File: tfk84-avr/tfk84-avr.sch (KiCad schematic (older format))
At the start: 31 parts, among them J1 USB_C_Receptacle_USB2.0, J2 AVR-ISP-6, SW1 Reset, U1 ATmega32U4-AU, Y1 16MHz

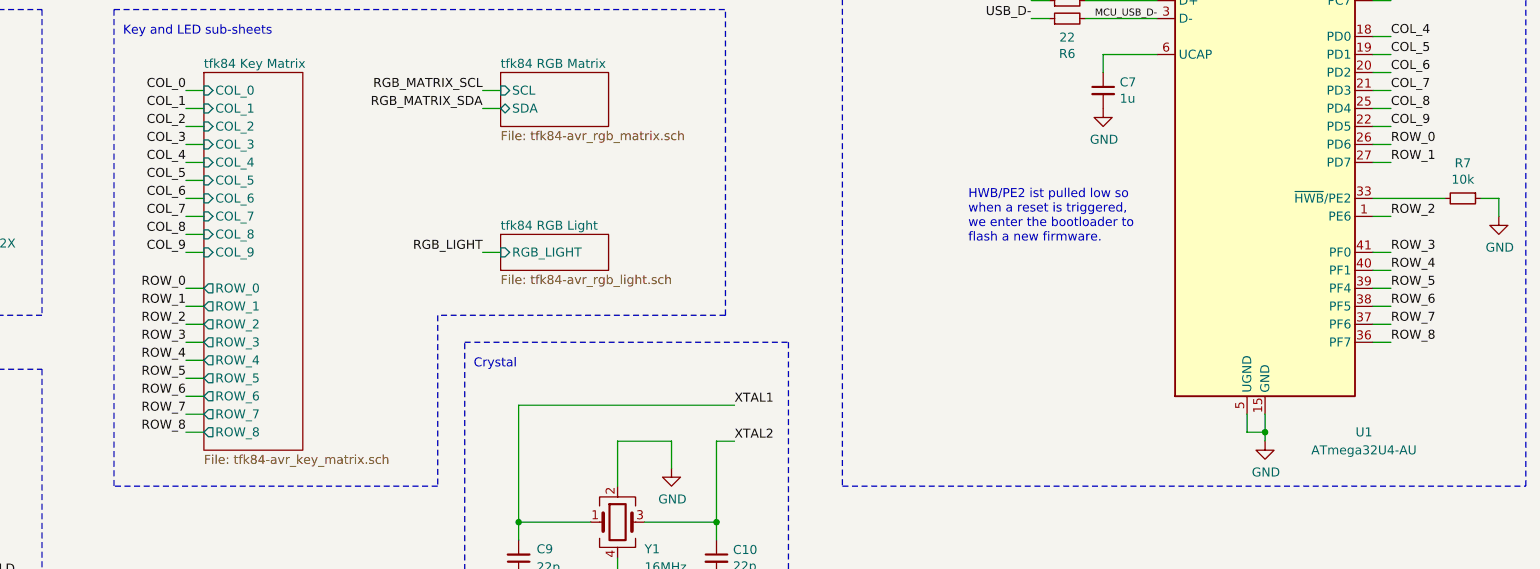
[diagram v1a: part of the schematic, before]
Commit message: Change key matrix to 12x7
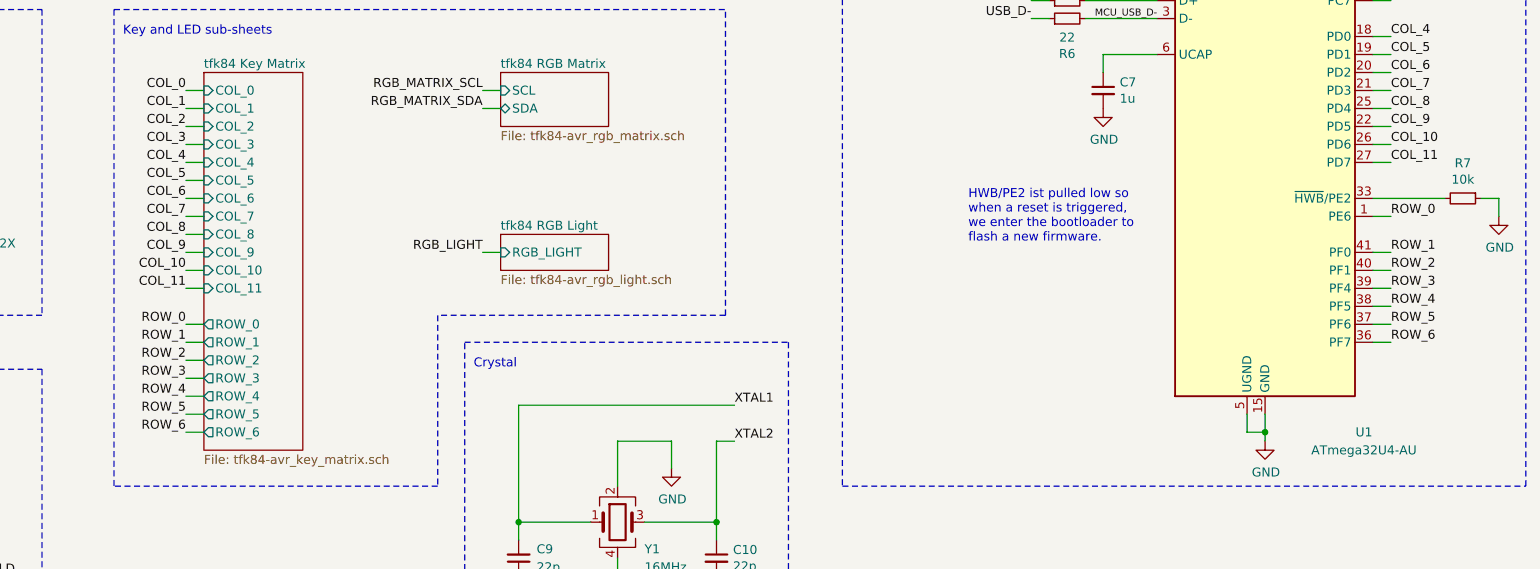
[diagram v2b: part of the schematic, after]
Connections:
- net ROW_7 is gone; now on net ROW_5: U1.37 (PF6)
- net ROW_8 is gone; now on net ROW_6: U1.36 (PF7)
- net ROW_0: now also U1.1 (PE6); no longer U1.26 (PD6)
- net ROW_1: now also U1.41 (PF0); no longer U1.27 (PD7)
- net ROW_2: now also U1.40 (PF1); no longer U1.1 (PE6)
- net ROW_3: now also U1.39 (PF4); no longer U1.41 (PF0)
- net ROW_4: now also U1.38 (PF5); no longer U1.40 (PF1)
- net ROW_5: no longer U1.39 (PF4)
- net ROW_6: no longer U1.38 (PF5)
- new net COL_10: U1.26 (PD6)
- new net COL_11: U1.27 (PD7)
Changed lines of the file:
@@
 	3550 4550 3450 4550
 Wire Wire Line
-	3550 5350 3450 5350
-Wire Wire Line
-	3550 5450 3450 5450
-Wire Wire Line
-	3450 5550 3550 5550
-Wire Wire Line
-	3550 5650 3450 5650
+	3550 5550 3450 5550
 Wire Wire Line
 	3450 5750 3550 5750
-Text Label 3450 5350 2    50   ~ 0
+Wire Wire Line
+	3550 5850 3450 5850
+Wire Wire Line
+	3450 5950 3550 5950
+Text Label 3450 5550 2    50   ~ 0
 ROW_0
-Text Label 3450 5450 2    50   ~ 0
+Text Label 3450 5650 2    50   ~ 0
 ROW_1
-Text Label 3450 5550 2    50   ~ 0
+Text Label 3450 5750 2    50   ~ 0
 ROW_2
-Text Label 3450 5650 2    50   ~ 0
+Text Label 3450 5850 2    50   ~ 0
 ROW_3
-Text Label 3450 5750 2    50   ~ 0
+Text Label 3450 5950 2    50   ~ 0
 ROW_4
 Text Label 3450 4250 2    50   ~ 0
@@
 	700  -250 700  -1250
 Wire Wire Line
-	3550 5850 3450 5850
-Text Label 3450 5850 2    50   ~ 0
+	3550 6050 3450 6050
+Text Label 3450 6050 2    50   ~ 0
 ROW_5
 Connection ~ 1150 2800
@@
 	10050 4150 10150 4150
 Text Label 10150 5650 0    50   ~ 0
-ROW_8
+ROW_6
+Text Label 10150 5350 0    50   ~ 0
+ROW_3
 Text Label 10150 5550 0    50   ~ 0
-ROW_7
+ROW_5
 Text Label 10150 5450 0    50   ~ 0
-ROW_6
+ROW_4
+Text Label 10150 5250 0    50   ~ 0
+ROW_2
 Text Label 10150 5150 0    50   ~ 0
-ROW_3
-Text Label 10150 5350 0    50   ~ 0
-ROW_5
-Text Label 10150 5250 0    50   ~ 0
-ROW_4
+ROW_1
 Text Label 10150 4950 0    50   ~ 0
-ROW_2
-Text Label 10150 4650 0    50   ~ 0
-ROW_1
-Text Label 10150 4550 0    50   ~ 0
 ROW_0
 $Sheet
@@
 F4 "COL_2" I L 3550 4450 50
 F5 "COL_3" I L 3550 4550 50
-F6 "ROW_0" O L 3550 5350 50
-F7 "ROW_1" O L 3550 5450 50
-F8 "ROW_2" O L 3550 5550 50
-F9 "ROW_3" O L 3550 5650 50
-F10 "ROW_4" O L 3550 5750 50
-F11 "ROW_5" O L 3550 5850 50
+F6 "ROW_0" O L 3550 5550 50
+F7 "ROW_1" O L 3550 5650 50
+F8 "ROW_2" O L 3550 5750 50
+F9 "ROW_3" O L 3550 5850 50
+F10 "ROW_4" O L 3550 5950 50
+F11 "ROW_5" O L 3550 6050 50
 F12 "COL_4" I L 3550 4650 50
 F13 "COL_5" I L 3550 4750 50
@@
 F16 "COL_8" I L 3550 5050 50
 F17 "COL_9" I L 3550 5150 50
-F18 "ROW_6" O L 3550 5950 50
-F19 "ROW_7" O L 3550 6050 50
-F20 "ROW_8" O L 3550 6150 50
+F18 "ROW_6" O L 3550 6150 50
+F19 "COL_10" I L 3550 5250 50
+F20 "COL_11" I L 3550 5350 50
 $EndSheet
-Wire Wire Line
-	3550 5950 3450 5950
-Wire Wire Line
-	3450 6050 3550 6050
-Wire Wire Line
-	3550 6150 3450 6150
-Text Label 3450 5950 2    50   ~ 0
-ROW_6
-Text Label 3450 6050 2    50   ~ 0
-ROW_7
-Text Label 3450 6150 2    50   ~ 0
-ROW_8
 Text Label 3450 4650 2    50   ~ 0
 COL_4
@@
 Wire Notes Line
 	3050 3800 3050 6450
+Text Label 3450 6150 2    50   ~ 0
+ROW_6
+Wire Wire Line
+	3450 6150 3550 6150
+Wire Wire Line
+	3450 5650 3550 5650
+Wire Wire Line
+	3450 5250 3550 5250
+Wire Wire Line
+	3450 5350 3550 5350
+Text Label 3450 5250 2    50   ~ 0
+COL_10
+Text Label 3450 5350 2    50   ~ 0
+COL_11
+Text Label 10150 4550 0    50   ~ 0
+COL_10
+Text Label 10150 4650 0    50   ~ 0
+COL_11
 $EndSCHEMATC

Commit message: Continue layout
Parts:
- added H10, H11, H9: MountingHole, MountingHole:MountingHole_2.5mm_Pad, symbol Mechanical:MountingHole
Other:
- moved on the sheet: C8, D3, H1, H2, H3, H4, R8
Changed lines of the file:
@@
 L Device:D_Small D3
 U 1 1 60989164
-P 1350 6550
+P 1500 6300
 AR Path="/60989164" Ref="D3"  Part="1"
 AR Path="/60815FFC/60989164" Ref="D?"  Part="1"
-F 0 "D3" H 1350 6450 50  0000 C CNN
-F 1 "Case ESD" H 1350 6434 50  0001 C CNN
-F 2 "Diode_SMD:D_SOD-123" V 1350 6550 50  0001 C CNN
-F 3 "~" V 1350 6550 50  0001 C CNN
-	1    1350 6550
+F 0 "D3" H 1500 6200 50  0000 C CNN
+F 1 "Case ESD" H 1500 6184 50  0001 C CNN
+F 2 "Diode_SMD:D_SOD-123" V 1500 6300 50  0001 C CNN
+F 3 "~" V 1500 6300 50  0001 C CNN
+	1    1500 6300
 	-1   0    0    1
 $EndComp
 Wire Wire Line
-	1450 6550 1550 6550
-Wire Wire Line
-	1550 6550 1550 6650
-Wire Wire Line
-	1550 6550 1900 6550
-Wire Wire Line
-	1900 6550 1900 6650
-Connection ~ 1550 6550
+	1600 6300 1700 6300
+Wire Wire Line
+	1700 6300 1700 6400
+Wire Wire Line
+	1700 6300 2050 6300
+Wire Wire Line
+	2050 6300 2050 6400
+Connection ~ 1700 6300
 $Comp
 L Device:R_Small R8
 U 1 1 6098916F
-P 1550 6750
+P 1700 6500
 AR Path="/6098916F" Ref="R8"  Part="1"
 AR Path="/60815FFC/6098916F" Ref="R?"  Part="1"
-F 0 "R8" H 1609 6796 50  0000 L CNN
-F 1 "1M" H 1609 6705 50  0000 L CNN
-F 2 "Resistor_SMD:R_0805_2012Metric_Pad1.20x1.40mm_HandSolder" H 1550 6750 50  0001 C CNN
-F 3 "~" H 1550 6750 50  0001 C CNN
-	1    1550 6750
+F 0 "R8" H 1759 6546 50  0000 L CNN
+F 1 "1M" H 1759 6455 50  0000 L CNN
+F 2 "Resistor_SMD:R_0805_2012Metric_Pad1.20x1.40mm_HandSolder" H 1700 6500 50  0001 C CNN
+F 3 "~" H 1700 6500 50  0001 C CNN
+	1    1700 6500
 	1    0    0    -1
 $EndComp
@@
 L Device:C_Small C8
 U 1 1 60989175
-P 1900 6750
+P 2050 6500
 AR Path="/60989175" Ref="C8"  Part="1"
 AR Path="/60815FFC/60989175" Ref="C?"  Part="1"
-F 0 "C8" H 1992 6796 50  0000 L CNN
-F 1 "4.7n" H 1992 6705 50  0000 L CNN
-F 2 "Capacitor_SMD:C_0805_2012Metric_Pad1.18x1.45mm_HandSolder" H 1900 6750 50  0001 C CNN
-F 3 "~" H 1900 6750 50  0001 C CNN
-	1    1900 6750
-	1    0    0    -1
-$EndComp
-Wire Wire Line
-	1900 6850 1900 6950
-Wire Wire Line
-	1900 6950 1550 6950
-Wire Wire Line
-	1550 6950 1550 6850
-Text Notes 750  5950 0    50   ~ 0
+F 0 "C8" H 2142 6546 50  0000 L CNN
+F 1 "4.7n" H 2142 6455 50  0000 L CNN
+F 2 "Capacitor_SMD:C_0805_2012Metric_Pad1.18x1.45mm_HandSolder" H 2050 6500 50  0001 C CNN
+F 3 "~" H 2050 6500 50  0001 C CNN
+	1    2050 6500
+	1    0    0    -1
+$EndComp
+Wire Wire Line
+	2050 6600 2050 6700
+Wire Wire Line
+	2050 6700 1700 6700
+Wire Wire Line
+	1700 6700 1700 6600
+Text Notes 900  5900 0    50   ~ 0
 Mounting holes and ESD inrush protection
 Wire Notes Line
-	700  5800 2650 5800
-Wire Notes Line
-	2650 5800 2650 7600
-Wire Notes Line
-	2650 7600 700  7600
-Wire Notes Line
-	700  7600 700  5800
-Wire Wire Line
-	1250 6550 1050 6550
+	700  5750 2800 5750
+Wire Notes Line
+	2800 5750 2800 7550
+Wire Notes Line
+	2800 7550 700  7550
+Wire Notes Line
+	700  7550 700  5750
+Wire Wire Line
+	1400 6300 1200 6300
 $Comp
 L Mechanical:MountingHole_Pad H2
 U 1 1 60989184
-P 950 6550
+P 1100 6300
 AR Path="/60989184" Ref="H2"  Part="1"
 AR Path="/60815FFC/60989184" Ref="H?"  Part="1"
-F 0 "H2" V 800 6600 50  0000 C CNN
-F 1 "Case" V 700 6600 50  0000 C CNN
-F 2 "MountingHole:MountingHole_2.5mm_Pad" H 950 6550 50  0001 C CNN
-F 3 "~" H 950 6550 50  0001 C CNN
-	1    950  6550
+F 0 "H2" V 1100 6500 50  0000 C CNN
+F 1 "Case" V 1000 6500 50  0000 C CNN
+F 2 "MountingHole:MountingHole_2.5mm_Pad" H 1100 6300 50  0001 C CNN
+F 3 "~" H 1100 6300 50  0001 C CNN
+	1    1100 6300
 	0    -1   -1   0
 $EndComp
 Wire Wire Line
-	1900 6950 2250 6950
-Connection ~ 1900 6950
-Text Label 2250 6950 0    50   ~ 0
+	2050 6700 2400 6700
+Connection ~ 2050 6700
+Text Label 2400 6700 0    50   ~ 0
 SHIELD
-Text Notes 1600 7300 0    50   ~ 0
+Text Notes 1750 7050 0    50   ~ 0
 Shunt ESD away from \nGND and ICs to USB \nshield.
 Wire Wire Line
@@
 L Mechanical:MountingHole H1
 U 1 1 60BC9C45
-P 900 6150
-F 0 "H1" H 850 6000 50  0000 L CNN
-F 1 "MountingHole" H 800 5900 50  0001 L CNN
-F 2 "MountingHole:MountingHole_2.5mm_Pad" H 900 6150 50  0001 C CNN
-F 3 "~" H 900 6150 50  0001 C CNN
-	1    900  6150
+P 1050 6100
+F 0 "H1" H 850 6100 50  0000 L CNN
+F 1 "MountingHole" H 950 5850 50  0001 L CNN
+F 2 "MountingHole:MountingHole_2.5mm_Pad" H 1050 6100 50  0001 C CNN
+F 3 "~" H 1050 6100 50  0001 C CNN
+	1    1050 6100
 	1    0    0    -1
 $EndComp
@@
 L Mechanical:MountingHole H3
 U 1 1 60BCA1EE
-P 900 6950
-F 0 "H3" H 850 6800 50  0000 L CNN
-F 1 "MountingHole" H 1000 6905 50  0001 L CNN
-F 2 "MountingHole:MountingHole_2.5mm_Pad" H 900 6950 50  0001 C CNN
-F 3 "~" H 900 6950 50  0001 C CNN
-	1    900  6950
+P 1050 6500
+F 0 "H3" H 850 6500 50  0000 L CNN
+F 1 "MountingHole" H 1150 6455 50  0001 L CNN
+F 2 "MountingHole:MountingHole_2.5mm_Pad" H 1050 6500 50  0001 C CNN
+F 3 "~" H 1050 6500 50  0001 C CNN
+	1    1050 6500
 	1    0    0    -1
 $EndComp
@@
 L Mechanical:MountingHole H4
 U 1 1 60BCA526
-P 900 7350
-F 0 "H4" H 850 7200 50  0000 L CNN
-F 1 "MountingHole" H 1000 7305 50  0001 L CNN
-F 2 "MountingHole:MountingHole_2.5mm_Pad" H 900 7350 50  0001 C CNN
-F 3 "~" H 900 7350 50  0001 C CNN
-	1    900  7350
+P 1050 6700
+F 0 "H4" H 850 6700 50  0000 L CNN
+F 1 "MountingHole" H 1150 6655 50  0001 L CNN
+F 2 "MountingHole:MountingHole_2.5mm_Pad" H 1050 6700 50  0001 C CNN
+F 3 "~" H 1050 6700 50  0001 C CNN
+	1    1050 6700
 	1    0    0    -1
 $EndComp
@@
 Text Label 10150 4650 0    50   ~ 0
 COL_11
+$Comp
+L Mechanical:MountingHole H9
+U 1 1 60FF3666
+P 1050 6900
+F 0 "H9" H 850 6900 50  0000 L CNN
+F 1 "MountingHole" H 1150 6855 50  0001 L CNN
+F 2 "MountingHole:MountingHole_2.5mm_Pad" H 1050 6900 50  0001 C CNN
+F 3 "~" H 1050 6900 50  0001 C CNN
+	1    1050 6900
+	1    0    0    -1
+$EndComp
+$Comp
+L Mechanical:MountingHole H10
+U 1 1 60FF38B8
+P 1050 7100
+F 0 "H10" H 800 7100 50  0000 L CNN
+F 1 "MountingHole" H 1150 7055 50  0001 L CNN
+F 2 "MountingHole:MountingHole_2.5mm_Pad" H 1050 7100 50  0001 C CNN
+F 3 "~" H 1050 7100 50  0001 C CNN
+	1    1050 7100
+	1    0    0    -1
+$EndComp
+$Comp
+L Mechanical:MountingHole H11
+U 1 1 60FF3AA3
+P 1050 7300
+F 0 "H11" H 800 7300 50  0000 L CNN
+F 1 "MountingHole" H 1150 7255 50  0001 L CNN
+F 2 "MountingHole:MountingHole_2.5mm_Pad" H 1050 7300 50  0001 C CNN
+F 3 "~" H 1050 7300 50  0001 C CNN
+	1    1050 7300
+	1    0    0    -1
+$EndComp
 $EndSCHEMATC

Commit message: Continue layout
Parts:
- H1: renamed from H2; footprint MountingHole:MountingHole_2.5mm_Pad -> MountingHole:MountingHole_2.5mm_Pad_TopOnly
- H10, H11, H3, H4, H9: footprint MountingHole:MountingHole_2.5mm_Pad -> MountingHole:MountingHole_2.5mm_Pad_TopOnly
- H2: renamed from H1; footprint MountingHole:MountingHole_2.5mm_Pad -> MountingHole:MountingHole_2.5mm_Pad_TopOnly
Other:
- moved on the sheet: C8, D3, H1, H2, R8
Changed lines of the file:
@@
 L Device:D_Small D3
 U 1 1 60989164
-P 1500 6300
+P 1500 6100
 AR Path="/60989164" Ref="D3"  Part="1"
 AR Path="/60815FFC/60989164" Ref="D?"  Part="1"
-F 0 "D3" H 1500 6200 50  0000 C CNN
-F 1 "Case ESD" H 1500 6184 50  0001 C CNN
-F 2 "Diode_SMD:D_SOD-123" V 1500 6300 50  0001 C CNN
-F 3 "~" V 1500 6300 50  0001 C CNN
-	1    1500 6300
+F 0 "D3" H 1500 6000 50  0000 C CNN
+F 1 "Case ESD" H 1500 5984 50  0001 C CNN
+F 2 "Diode_SMD:D_SOD-123" V 1500 6100 50  0001 C CNN
+F 3 "~" V 1500 6100 50  0001 C CNN
+	1    1500 6100
 	-1   0    0    1
 $EndComp
 Wire Wire Line
-	1600 6300 1700 6300
-Wire Wire Line
-	1700 6300 1700 6400
-Wire Wire Line
-	1700 6300 2050 6300
-Wire Wire Line
-	2050 6300 2050 6400
-Connection ~ 1700 6300
+	1600 6100 1700 6100
+Wire Wire Line
+	1700 6100 1700 6200
+Wire Wire Line
+	1700 6100 2050 6100
+Wire Wire Line
+	2050 6100 2050 6200
+Connection ~ 1700 6100
 $Comp
 L Device:R_Small R8
 U 1 1 6098916F
-P 1700 6500
+P 1700 6300
 AR Path="/6098916F" Ref="R8"  Part="1"
 AR Path="/60815FFC/6098916F" Ref="R?"  Part="1"
-F 0 "R8" H 1759 6546 50  0000 L CNN
-F 1 "1M" H 1759 6455 50  0000 L CNN
-F 2 "Resistor_SMD:R_0805_2012Metric_Pad1.20x1.40mm_HandSolder" H 1700 6500 50  0001 C CNN
-F 3 "~" H 1700 6500 50  0001 C CNN
-	1    1700 6500
+F 0 "R8" H 1759 6346 50  0000 L CNN
+F 1 "1M" H 1759 6255 50  0000 L CNN
+F 2 "Resistor_SMD:R_0805_2012Metric_Pad1.20x1.40mm_HandSolder" H 1700 6300 50  0001 C CNN
+F 3 "~" H 1700 6300 50  0001 C CNN
+	1    1700 6300
 	1    0    0    -1
 $EndComp
@@
 L Device:C_Small C8
 U 1 1 60989175
-P 2050 6500
+P 2050 6300
 AR Path="/60989175" Ref="C8"  Part="1"
 AR Path="/60815FFC/60989175" Ref="C?"  Part="1"
-F 0 "C8" H 2142 6546 50  0000 L CNN
-F 1 "4.7n" H 2142 6455 50  0000 L CNN
-F 2 "Capacitor_SMD:C_0805_2012Metric_Pad1.18x1.45mm_HandSolder" H 2050 6500 50  0001 C CNN
-F 3 "~" H 2050 6500 50  0001 C CNN
-	1    2050 6500
-	1    0    0    -1
-$EndComp
-Wire Wire Line
-	2050 6600 2050 6700
-Wire Wire Line
-	2050 6700 1700 6700
-Wire Wire Line
-	1700 6700 1700 6600
+F 0 "C8" H 2142 6346 50  0000 L CNN
+F 1 "4.7n" H 2142 6255 50  0000 L CNN
+F 2 "Capacitor_SMD:C_0805_2012Metric_Pad1.18x1.45mm_HandSolder" H 2050 6300 50  0001 C CNN
+F 3 "~" H 2050 6300 50  0001 C CNN
+	1    2050 6300
+	1    0    0    -1
+$EndComp
+Wire Wire Line
+	2050 6400 2050 6500
+Wire Wire Line
+	2050 6500 1700 6500
+Wire Wire Line
+	1700 6500 1700 6400
 Text Notes 900  5900 0    50   ~ 0
 Mounting holes and ESD inrush protection
@@
 	700  7550 700  5750
 Wire Wire Line
-	1400 6300 1200 6300
-$Comp
-L Mechanical:MountingHole_Pad H2
+	1400 6100 1200 6100
+$Comp
+L Mechanical:MountingHole_Pad H1
 U 1 1 60989184
-P 1100 6300
-AR Path="/60989184" Ref="H2"  Part="1"
+P 1100 6100
+AR Path="/60989184" Ref="H1"  Part="1"
 AR Path="/60815FFC/60989184" Ref="H?"  Part="1"
-F 0 "H2" V 1100 6500 50  0000 C CNN
-F 1 "Case" V 1000 6500 50  0000 C CNN
-F 2 "MountingHole:MountingHole_2.5mm_Pad" H 1100 6300 50  0001 C CNN
-F 3 "~" H 1100 6300 50  0001 C CNN
-	1    1100 6300
+F 0 "H1" V 1100 6300 50  0000 C CNN
+F 1 "Case" V 1000 6300 50  0000 C CNN
+F 2 "MountingHole:MountingHole_2.5mm_Pad_TopOnly" H 1100 6100 50  0001 C CNN
+F 3 "~" H 1100 6100 50  0001 C CNN
+	1    1100 6100
 	0    -1   -1   0
 $EndComp
 Wire Wire Line
-	2050 6700 2400 6700
-Connection ~ 2050 6700
-Text Label 2400 6700 0    50   ~ 0
+	2050 6500 2400 6500
+Connection ~ 2050 6500
+Text Label 2400 6500 0    50   ~ 0
 SHIELD
-Text Notes 1750 7050 0    50   ~ 0
+Text Notes 1750 6850 0    50   ~ 0
 Shunt ESD away from \nGND and ICs to USB \nshield.
 Wire Wire Line
@@
 	3000 1250 2400 1250
 $Comp
-L Mechanical:MountingHole H1
+L Mechanical:MountingHole H2
 U 1 1 60BC9C45
-P 1050 6100
-F 0 "H1" H 850 6100 50  0000 L CNN
-F 1 "MountingHole" H 950 5850 50  0001 L CNN
-F 2 "MountingHole:MountingHole_2.5mm_Pad" H 1050 6100 50  0001 C CNN
-F 3 "~" H 1050 6100 50  0001 C CNN
-	1    1050 6100
+P 1050 6300
+F 0 "H2" H 850 6300 50  0000 L CNN
+F 1 "MountingHole" H 950 6050 50  0001 L CNN
+F 2 "MountingHole:MountingHole_2.5mm_Pad_TopOnly" H 1050 6300 50  0001 C CNN
+F 3 "~" H 1050 6300 50  0001 C CNN
+	1    1050 6300
 	1    0    0    -1
 $EndComp
@@
 F 0 "H3" H 850 6500 50  0000 L CNN
 F 1 "MountingHole" H 1150 6455 50  0001 L CNN
-F 2 "MountingHole:MountingHole_2.5mm_Pad" H 1050 6500 50  0001 C CNN
+F 2 "MountingHole:MountingHole_2.5mm_Pad_TopOnly" H 1050 6500 50  0001 C CNN
 F 3 "~" H 1050 6500 50  0001 C CNN
 	1    1050 6500
@@
 F 0 "H4" H 850 6700 50  0000 L CNN
 F 1 "MountingHole" H 1150 6655 50  0001 L CNN
-F 2 "MountingHole:MountingHole_2.5mm_Pad" H 1050 6700 50  0001 C CNN
+F 2 "MountingHole:MountingHole_2.5mm_Pad_TopOnly" H 1050 6700 50  0001 C CNN
 F 3 "~" H 1050 6700 50  0001 C CNN
 	1    1050 6700
@@
 F 0 "H9" H 850 6900 50  0000 L CNN
 F 1 "MountingHole" H 1150 6855 50  0001 L CNN
-F 2 "MountingHole:MountingHole_2.5mm_Pad" H 1050 6900 50  0001 C CNN
+F 2 "MountingHole:MountingHole_2.5mm_Pad_TopOnly" H 1050 6900 50  0001 C CNN
 F 3 "~" H 1050 6900 50  0001 C CNN
 	1    1050 6900
@@
 F 0 "H10" H 800 7100 50  0000 L CNN
 F 1 "MountingHole" H 1150 7055 50  0001 L CNN
-F 2 "MountingHole:MountingHole_2.5mm_Pad" H 1050 7100 50  0001 C CNN
+F 2 "MountingHole:MountingHole_2.5mm_Pad_TopOnly" H 1050 7100 50  0001 C CNN
 F 3 "~" H 1050 7100 50  0001 C CNN
 	1    1050 7100
@@
 F 0 "H11" H 800 7300 50  0000 L CNN
 F 1 "MountingHole" H 1150 7255 50  0001 L CNN
-F 2 "MountingHole:MountingHole_2.5mm_Pad" H 1050 7300 50  0001 C CNN
+F 2 "MountingHole:MountingHole_2.5mm_Pad_TopOnly" H 1050 7300 50  0001 C CNN
 F 3 "~" H 1050 7300 50  0001 C CNN
 	1    1050 7300
